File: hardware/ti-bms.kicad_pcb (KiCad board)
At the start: 2 copper layers, 93.5 x 53 mm, 68 parts, among them J1 Conn_02x03_Odd_Even, J2 Conn_01x02, J3 Conn_01x02, J4 Conn_01x02, J5 CAN_TERM, J6 Conn_01x02, U1 Pico, U10 SN74LV1T34DBV, U2 MCP2515-xST, U3 SN65HVD231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

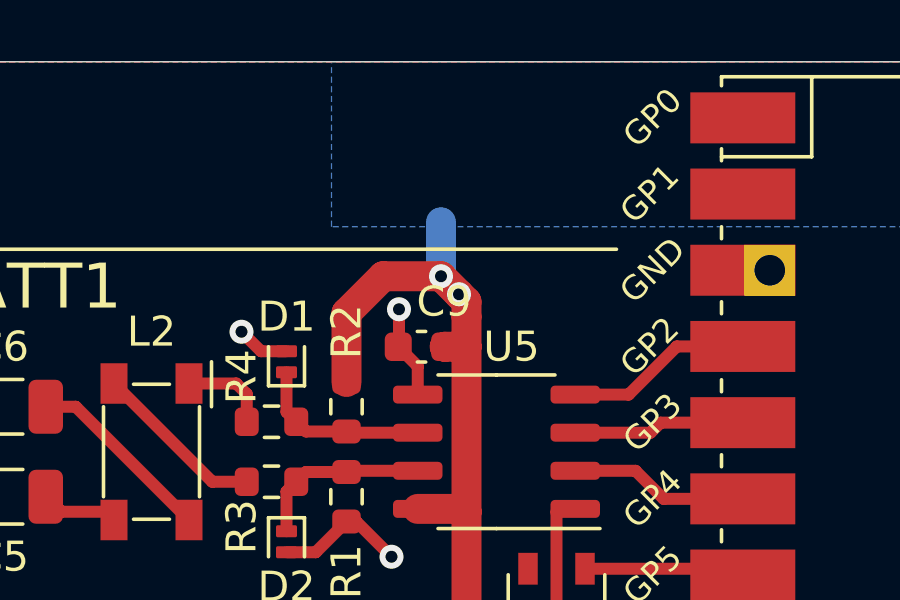
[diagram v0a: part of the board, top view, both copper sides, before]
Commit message: add missing trace
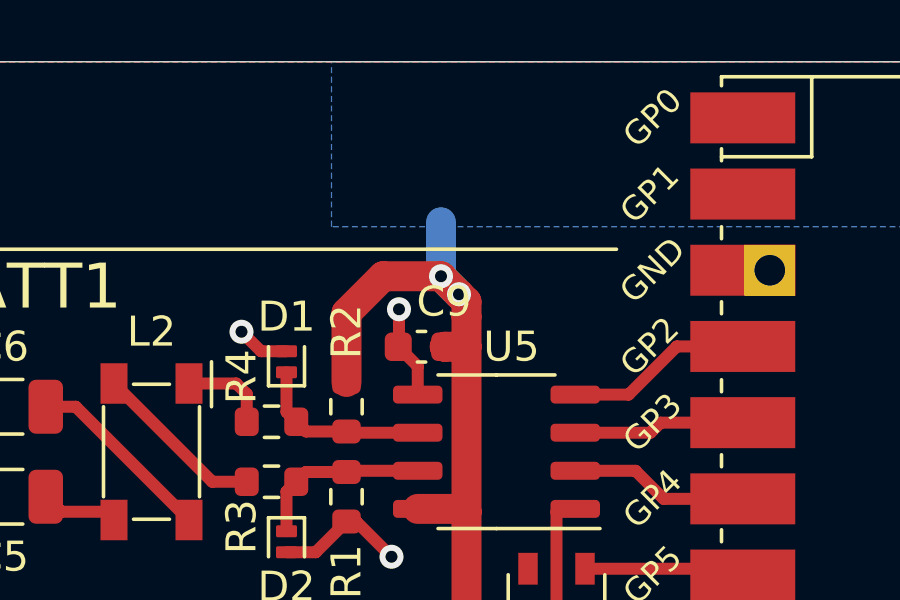
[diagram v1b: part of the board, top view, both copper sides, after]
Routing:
- net +5V: track 80.1 -> 81.0 mm

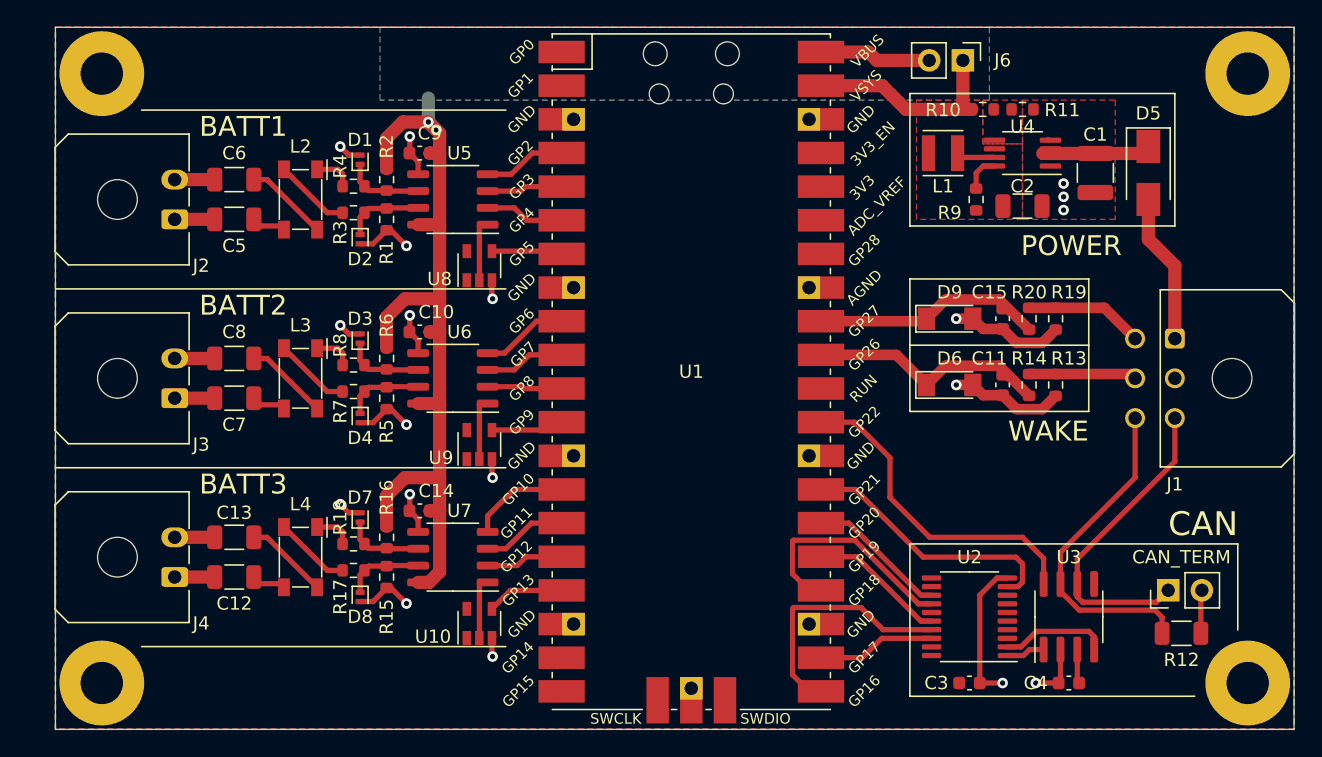
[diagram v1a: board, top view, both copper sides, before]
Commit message: integrate transformer for more common mode rejection
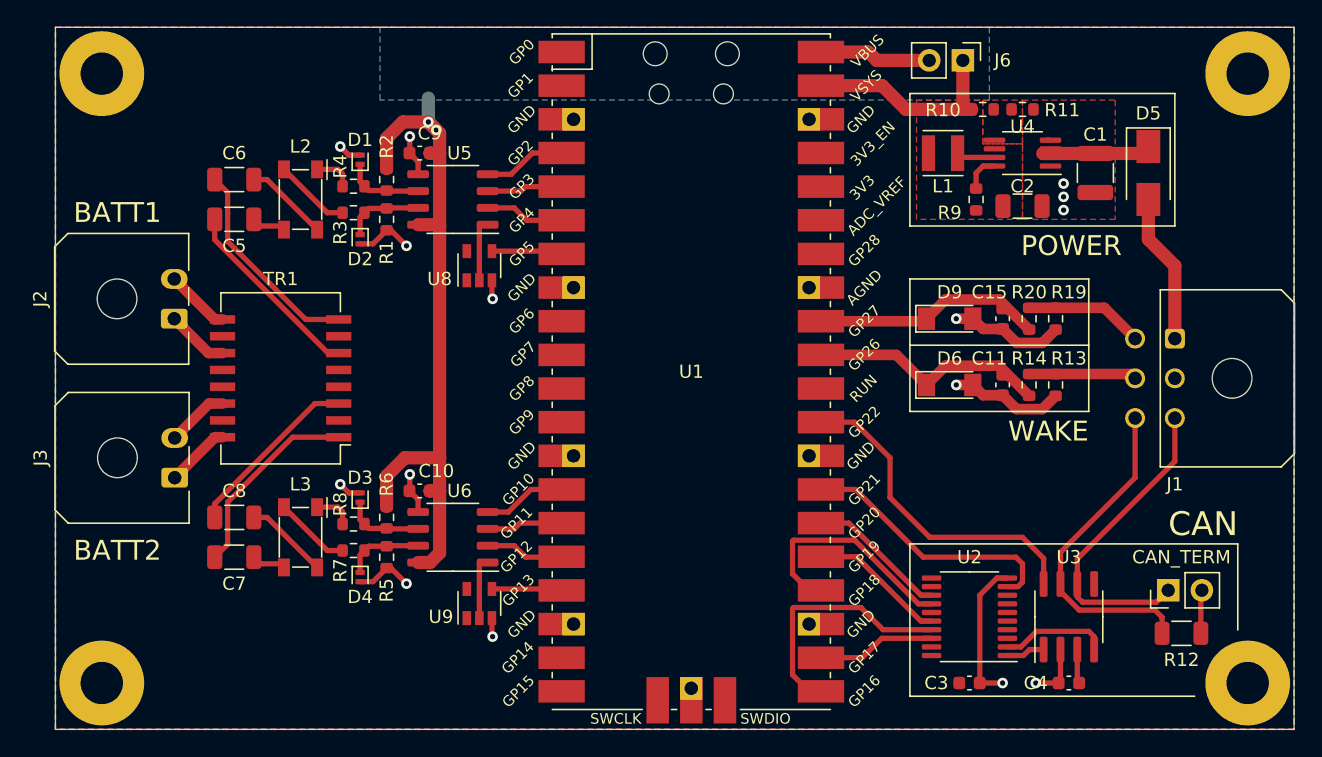
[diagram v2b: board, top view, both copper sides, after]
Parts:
- removed C12, C13: 10n 1000v, Capacitor_SMD:C_1206_3216Metric
- removed C14: 100n, Capacitor_SMD:C_0603_1608Metric
- removed D7, D8: 5v, footprints:SOD882
- removed J4: Conn_01x02, Connector_Molex:Molex_Micro-Fit_3.0_43650-0200_1x02_P3.00mm_Horizontal
- removed L4: 51uH, footprints:ACT45B-101-2P-TL003
- removed R15, R16: 1k, Resistor_SMD:R_0603_1608Metric
- removed R17, R18: 10, Resistor_SMD:R_0603_1608Metric
- removed U10: SN74LV1T34DBV, Package_TO_SOT_SMD:SOT-23-5
- removed U7: ISL8485EIBZ, Package_SO:SOP-8_3.9x4.9mm_P1.27mm
- added G***: LOGO, footprints:sc, B.Cu at (129.5, 73.5)
- added TR1: SM13072APEL, Transformer_SMD:Transformer_Ethernet_Wuerth_749013011A, F.Cu at (99.5, 88.5)
- R1, R2, R5, R6: value 1k -> 4k7
- moved C10 12.0 mm to (110.0, 97.0)
- moved C7 12.0 mm to (96.0, 102.0)
- moved C8 12.0 mm to (96.0, 99.0)
- moved D3 12.0 mm to (105.5, 97.5)
- moved D4 12.0 mm to (105.5, 103.5)
- moved L3 12.0 mm to (101.0, 100.5)
- moved R5 12.0 mm to (107.5, 102.0)
- moved R6 12.0 mm to (107.5, 99.0)
- moved R7 12.0 mm to (105.0, 101.5)
- moved R8 12.0 mm to (105.0, 99.5)
- moved U6 12.0 mm to (112.5, 100.5)
- moved U9 12.0 mm to (114.5, 105.5)
- moved J2 7.50 mm to (91.5, 84.0)
- moved J3 6.00 mm to (91.5, 96.0)
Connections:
- C5 pad 1: B1- -> Net-(C5-Pad1)
- C6 pad 1: B1+ -> Net-(C6-Pad1)
- C7 pad 1: B2- -> Net-(C7-Pad1)
- C8 pad 1: B2+ -> Net-(C8-Pad1)
- U1 pad 1: (no net) -> unconnected-(U1-Pad1)
- U1 pad 10: TXE_2 -> unconnected-(U1-Pad10)
- U1 pad 11: RXE_2 -> unconnected-(U1-Pad11)
- U1 pad 12: RXD_2 -> unconnected-(U1-Pad12)
- U1 pad 14: TXD_3 -> TXD_2
- U1 pad 15: TXE_3 -> TXE_2
- U1 pad 16: RXE_3 -> RXE_2
- U1 pad 17: RXD_3 -> RXD_2
- U1 pad 19: (no net) -> unconnected-(U1-Pad19)
- U1 pad 2: (no net) -> unconnected-(U1-Pad2)
- U1 pad 20: (no net) -> unconnected-(U1-Pad20)
- U1 pad 30: (no net) -> unconnected-(U1-Pad30)
- U1 pad 34: (no net) -> unconnected-(U1-Pad34)
- U1 pad 35: (no net) -> unconnected-(U1-Pad35)
- U1 pad 37: (no net) -> unconnected-(U1-Pad37)
- U1 pad 41: (no net) -> unconnected-(U1-Pad41)
- U1 pad 43: (no net) -> unconnected-(U1-Pad43)
- U1 pad 9: TXD_2 -> unconnected-(U1-Pad9)
- U2 pad 11: (no net) -> unconnected-(U2-Pad11)
- U2 pad 12: (no net) -> unconnected-(U2-Pad12)
- U2 pad 15: (no net) -> unconnected-(U2-Pad15)
- U2 pad 3: (no net) -> unconnected-(U2-Pad3)
- U2 pad 4: (no net) -> unconnected-(U2-Pad4)
- U2 pad 5: (no net) -> unconnected-(U2-Pad5)
- U2 pad 6: (no net) -> unconnected-(U2-Pad6)
- U2 pad 7: (no net) -> unconnected-(U2-Pad7)
- U2 pad 8: (no net) -> unconnected-(U2-Pad8)
- U3 pad 5: (no net) -> unconnected-(U3-Pad5)
- U8 pad 1: (no net) -> unconnected-(U8-Pad1)
- U9 pad 1: (no net) -> unconnected-(U9-Pad1)
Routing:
- net Net-(C6-Pad1): track 0.00 -> 15.9 mm
- net Net-(C7-Pad1): track 0.00 -> 15.0 mm
- net Net-(C5-Pad1): track 0.00 -> 14.4 mm
- net Net-(C8-Pad1): track 0.00 -> 13.5 mm
- net GND: track 64.9 -> 54.1 mm, vias 19 -> 15
- net +5V: track 81.0 -> 70.3 mm
- net TXD_3: track 8.53 -> 0.00 mm
- net TXE_3: track 7.29 -> 0.00 mm
- net RXE_3: track 6.76 -> 0.00 mm
- net RXD_3: track 6.74 -> 0.00 mm
- net Net-(C13-Pad2): track 6.34 -> 0.00 mm
- net Net-(D8-Pad1): track 5.99 -> 0.00 mm
- net Net-(D7-Pad1): track 5.99 -> 0.00 mm
- net Net-(L4-Pad2): track 5.78 -> 0.00 mm
- net Net-(U10-Pad2): track 4.76 -> 0.00 mm
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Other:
- net class Default removed
- net class Diff removed
- net class ExtraClearance removed
- board text added: "Daisychain BMS v5"
- board text removed: "BATT3"
- board text removed: "Daisychain BMS v4"
